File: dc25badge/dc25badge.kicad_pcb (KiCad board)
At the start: 2 copper layers, 111 parts, among them P1 BATT, P2 USB_OTG, P3 CONN_CORTEX, P4 UART, SW1 RESET, SW2 PWR, SW3 MODE, SW4 BRIGHT, U1 MIC5305, U10 APA102, U11 APA102, U12 APA102, U13 APA102, U14 APA102, U15 APA102, U16 APA102, U17 APA102, U18 APA102, U19 APA102, U2 TPS61232, U20 APA102, U21 APA102, U22 APA102, U23 APA102, U24 APA102, U25 APA102, U26 APA102, U27 APA102, U28 APA102, U29 APA102, U3 ATSAMD21E18A-AU, U30 APA102, U31 APA102, U32 APA102, U33 APA102, U34 APA102, U35 APA102, U36 APA102, U37 APA102, U38 APA102, U39 APA102, U4 74AHCT125, U40 APA102, U41 APA102, U42 APA102, U43 APA102, U44 APA102, U45 APA102, U46 APA102, U47 APA102, U48 APA102, U49 APA102, U5 APA102, U50 APA102, U51 APA102, U52 APA102, U53 APA102, U54 APA102, U55 APA102, U56 APA102, U57 APA102, U58 APA102, U59 APA102, U6 APA102, U60 APA102, U61 APA102, U62 APA102, U63 APA102, U64 APA102, U7 APA102, U8 APA102, U9 APA102, Y1 32.768k

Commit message: Full routing.
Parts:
- removed P4: UART, Pin_Headers2:Pin_Header_Straight_1x03_Pitch2.54mm_SMD_Pin1Left
- C15, C16, C17, C18, C19, C20, C21, C22, C23, C24, C25, C26, C8, R5, R6, SW1, SW2, SW3, SW4: moved to B.Cu
- moved C22 207.7 mm to (42.3, 28.8)
- moved C25 184.1 mm to (61.0, 57.1), turned to 270 degrees
- moved C23 178.7 mm to (48.4, 79.0)
- moved C26 174.5 mm to (52.2, 68.2), turned to 270 degrees
- moved C20 171.2 mm to (57.7, 79.0), turned to 180 degrees
- moved C15 148.7 mm to (101.2, 67.8), turned to 270 degrees
- moved C16 139.4 mm to (110.2, 56.9), turned to 270 degrees
- moved C17 132.2 mm to (96.9, 78.9)
- moved C18 131.9 mm to (137.8, 32.0)
- moved C19 127.8 mm to (106.7, 78.9), turned to 180 degrees
- moved SW4 116.3 mm to (68.7, 70.6)
- moved C21 111.2 mm to (161.7, 35.1), turned to 180 degrees
- moved SW1 100.6 mm to (101.2, 44.1), turned to 180 degrees
- moved C24 100.6 mm to (139.2, 83.8), turned to 180 degrees
- moved SW3 100.3 mm to (68.7, 62.4)
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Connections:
- net USBDM renamed USBD-
- net USBDP renamed USBD+
- P2 pad 6: Net-(P2-Pad6) -> GND
- U3 pad 25: Net-(U3-Pad25) -> 5V_EN
- U3 pad 5: 5V_EN -> Net-(U3-Pad5)
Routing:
- net +5V: track 34.2 -> 251.9 mm, vias 8 -> 30
- net 5V_EN: track 0.00 -> 95.0 mm, vias 0 -> 4
- net GND: track 112.9 -> 201.8 mm, vias 59 -> 60
- net /VBAT: track 0.00 -> 85.5 mm
- net +3V3: track 0.00 -> 59.4 mm
- net SPI_MOSI: track 0.00 -> 42.6 mm, vias 0 -> 1
- net BRIGHT: track 0.00 -> 37.6 mm
- net SPI_CLK: track 0.00 -> 35.6 mm, vias 0 -> 1
- net SPI_EN: track 0.00 -> 33.0 mm, vias 0 -> 2
- net MODE: track 0.00 -> 32.1 mm, vias 0 -> 2
- net ~RESET: track 0.00 -> 30.0 mm, vias 0 -> 2
- net Net-(R5-Pad2): track 0.00 -> 26.5 mm
- net SOFT_PWR: track 0.00 -> 23.1 mm, vias 0 -> 2
- net SCLK3: track 0.00 -> 17.9 mm
- net MOSI3: track 0.00 -> 16.7 mm
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- added copper zone on B.Cu, net +3V3
- added copper zone on B.Cu, net +5V
- added copper zone on B.Cu, net /VBAT
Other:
- rule trace_min: 0.254 -> 0.1524

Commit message: Gerbers.
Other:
- board outline added: 150.7 x 59.7 mm
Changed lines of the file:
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@@
     (links 358)
     (no_connects 0)
-    (area 0 0 0 0)
+    (area 26.344399 24.9826 177.683228 89.1374)
     (thickness 1.6)
-    (drawings 0)
+    (drawings 5)
     (tracks 1201)
     (zones 0)
@@
   (page A4)
   (layers
-    (0 F.Cu signal)
+    (0 F.Cu signal hide)
     (31 B.Cu signal)
     (32 B.Adhes user)
@@
     (visible_elements FFFFFF7F)
     (pcbplotparams
-      (layerselection 0x00030_80000001)
+      (layerselection 0x010f0_80000001)
       (usegerberextensions false)
       (excludeedgelayer true)
@@
       (plotinvisibletext false)
       (padsonsilk false)
-      (subtractmaskfromsilk false)
+      (subtractmaskfromsilk true)
       (outputformat 1)
       (mirror false)
-      (drillshape 1)
+      (drillshape 0)
       (scaleselection 1)
-      (outputdirectory ""))
+      (outputdirectory output/))
   )
   (net 0 "")
@@
     )
   )
+  (gr_line (start 26.67 86.868) (end 44.323 56.515) (angle 90) (layer Edge.Cuts) (width 0.15))
+  (gr_line (start 158.496 86.868) (end 26.67 86.868) (angle 90) (layer Edge.Cuts) (width 0.15))
+  (gr_line (start 177.419 27.178) (end 158.496 86.868) (angle 90) (layer Edge.Cuts) (width 0.15))
+  (gr_line (start 27.305 27.178) (end 177.419 27.178) (angle 90) (layer Edge.Cuts) (width 0.15))
+  (gr_line (start 44.323 56.515) (end 27.305 27.178) (angle 90) (layer Edge.Cuts) (width 0.15))
   (segment (start 78.008 31.369) (end 78.008 32.796) (width 0.254) (layer B.Cu) (net 1))
   (segment (start 78.008 32.796) (end 78.867 33.655) (width 0.254) (layer B.Cu) (net 1))

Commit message: PCB roll 1.
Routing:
- net GND: track 201.8 -> 242.4 mm
- net +5V: track 251.9 -> 257.1 mm, vias 30 -> 32
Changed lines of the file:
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@@
     (links 358)
     (no_connects 0)
-    (area 26.344399 24.9826 177.683228 89.1374)
+    (area 26.594999 27.102999 177.494001 86.943001)
     (thickness 1.6)
     (drawings 5)
-    (tracks 1201)
+    (tracks 1221)
     (zones 0)
     (modules 110)
@@
   (page A4)
   (layers
-    (0 F.Cu signal hide)
+    (0 F.Cu signal)
     (31 B.Cu signal)
     (32 B.Adhes user)
@@
   )
   (setup
-    (last_trace_width 1.016)
+    (last_trace_width 0.762)
     (user_trace_width 0.1524)
     (user_trace_width 0.254)
@@
   (gr_line (start 27.305 27.178) (end 177.419 27.178) (angle 90) (layer Edge.Cuts) (width 0.15))
   (gr_line (start 44.323 56.515) (end 27.305 27.178) (angle 90) (layer Edge.Cuts) (width 0.15))
+  (segment (start 145.542 43.962) (end 143.51 43.962) (width 0.762) (layer B.Cu) (net 1) (status C00000))
+  (segment (start 147.574 43.962) (end 145.542 43.962) (width 0.762) (layer B.Cu) (net 1) (status C00000))
+  (segment (start 150.007 44.196) (end 147.808 44.196) (width 0.762) (layer B.Cu) (net 1) (status C00000))
+  (segment (start 147.808 44.196) (end 147.574 43.962) (width 0.762) (layer B.Cu) (net 1) (status C00000))
+  (segment (start 150.007 44.196) (end 150.007 41.883) (width 0.762) (layer B.Cu) (net 1) (status C00000))
+  (segment (start 150.007 41.883) (end 149.907 41.783) (width 0.762) (layer B.Cu) (net 1) (status C00000))
+  (segment (start 151.257 47.498) (end 151.257 45.446) (width 0.762) (layer B.Cu) (net 1) (status 400000))
+  (segment (start 151.257 45.446) (end 150.007 44.196) (width 0.762) (layer B.Cu) (net 1) (status 800000))
+  (segment (start 151.257 47.498) (end 151.257 55.245) (width 1.016) (layer B.Cu) (net 1) (status 400000))
+  (segment (start 156.337 54.991) (end 156.337 50.018) (width 1.016) (layer B.Cu) (net 1) (status 800000))
+  (segment (start 156.464 55.118) (end 156.337 54.991) (width 1.016) (layer B.Cu) (net 1))
+  (segment (start 151.384 55.118) (end 156.464 55.118) (width 1.016) (layer B.Cu) (net 1))
+  (segment (start 151.257 55.245) (end 151.384 55.118) (width 1.016) (layer B.Cu) (net 1))
+  (segment (start 69.918 41.878) (end 74.2 41.878) (width 0.508) (layer B.Cu) (net 1) (status 400000))
+  (segment (start 76.6 39.478) (end 78.418 39.478) (width 0.508) (layer B.Cu) (net 1) (status 800000))
+  (segment (start 74.2 41.878) (end 76.6 39.478) (width 0.508) (layer B.Cu) (net 1))
   (segment (start 78.008 31.369) (end 78.008 32.796) (width 0.254) (layer B.Cu) (net 1))
   (segment (start 78.008 32.796) (end 78.867 33.655) (width 0.254) (layer B.Cu) (net 1))
@@
   (segment (start 84.639 41.078) (end 85.267 41.078) (width 0.508) (layer B.Cu) (net 3))
   (segment (start 85.267 41.078) (end 86.487 39.858) (width 0.508) (layer B.Cu) (net 3))
+  (segment (start 145.288 51.816) (end 145.288 54.61) (width 1.016) (layer B.Cu) (net 4) (status 400000))
+  (via (at 145.288 54.61) (size 1.016) (drill 0.508) (layers F.Cu B.Cu) (net 4))
+  (segment (start 145.288 51.816) (end 145.288 48.006) (width 1.016) (layer B.Cu) (net 4) (status 400000))
+  (via (at 143.891 49.276) (size 1.016) (drill 0.508) (layers F.Cu B.Cu) (net 4))
+  (segment (start 138.175 49.95) (end 139.153 49.95) (width 1.016) (layer F.Cu) (net 4) (status 400000))
+  (segment (start 138.946 43.95) (end 141.859 46.863) (width 0.508) (layer F.Cu) (net 4))
+  (via (at 141.859 46.863) (size 1.016) (drill 0.508) (layers F.Cu B.Cu) (net 4))
+  (segment (start 138.946 43.95) (end 136.675 43.95) (width 0.508) (layer F.Cu) (net 4))
+  (segment (start 141.859 47.244) (end 141.859 46.863) (width 1.016) (layer B.Cu) (net 4))
+  (segment (start 140.335 48.768) (end 141.859 47.244) (width 1.016) (layer B.Cu) (net 4))
+  (via (at 140.335 48.768) (size 1.016) (drill 0.508) (layers F.Cu B.Cu) (net 4))
+  (segment (start 139.153 49.95) (end 140.335 48.768) (width 1.016) (layer F.Cu) (net 4))
   (segment (start 140.569 83.693) (end 142.621 83.693) (width 1.016) (layer B.Cu) (net 4))
   (segment (start 146.431 79.883) (end 142.621 83.693) (width 2.54) (layer B.Cu) (net 4))
@@
   (segment (start 145.288 51.816) (end 145.288 49.276) (width 0.508) (layer B.Cu) (net 4))
   (segment (start 145.288 48.24) (end 143.51 46.462) (width 0.508) (layer B.Cu) (net 4))
-  (segment (start 136.675 43.95) (end 138.946 43.95) (width 0.508) (layer F.Cu) (net 4))
-  (via (at 141.859 46.863) (size 1.016) (drill 0.508) (layers F.Cu B.Cu) (net 4))
-  (segment (start 138.946 43.95) (end 141.859 46.863) (width 0.508) (layer F.Cu) (net 4))
   (segment (start 138.175 49.95) (end 141.312 49.95) (width 0.508) (layer F.Cu) (net 4))
   (via (at 141.986 49.276) (size 1.016) (drill 0.508) (layers F.Cu B.Cu) (net 4))
@@
   (segment (start 104.002 58.05) (end 104.013 58.039) (width 1.016) (layer F.Cu) (net 4))
   (segment (start 51.175 55.95) (end 49.346 55.95) (width 1.016) (layer F.Cu) (net 4))
-  (segment (start 45.223 58.05) (end 46.825 58.05) (width 1.016) (layer F.Cu) (net 4))
-  (segment (start 45.212 58.039) (end 45.223 58.05) (width 0.508) (layer F.Cu) (net 4))
-  (via (at 45.212 58.039) (size 1.016) (drill 0.508) (layers F.Cu B.Cu) (net 4))
-  (segment (start 47.117 58.039) (end 45.212 58.039) (width 1.016) (layer B.Cu) (net 4))
-  (segment (start 49.276 55.88) (end 47.117 58.039) (width 1.016) (layer B.Cu) (net 4))
   (via (at 49.276 55.88) (size 1.016) (drill 0.508) (layers F.Cu B.Cu) (net 4))
   (segment (start 49.346 55.95) (end 49.276 55.88) (width 0.508) (layer F.Cu) (net 4))

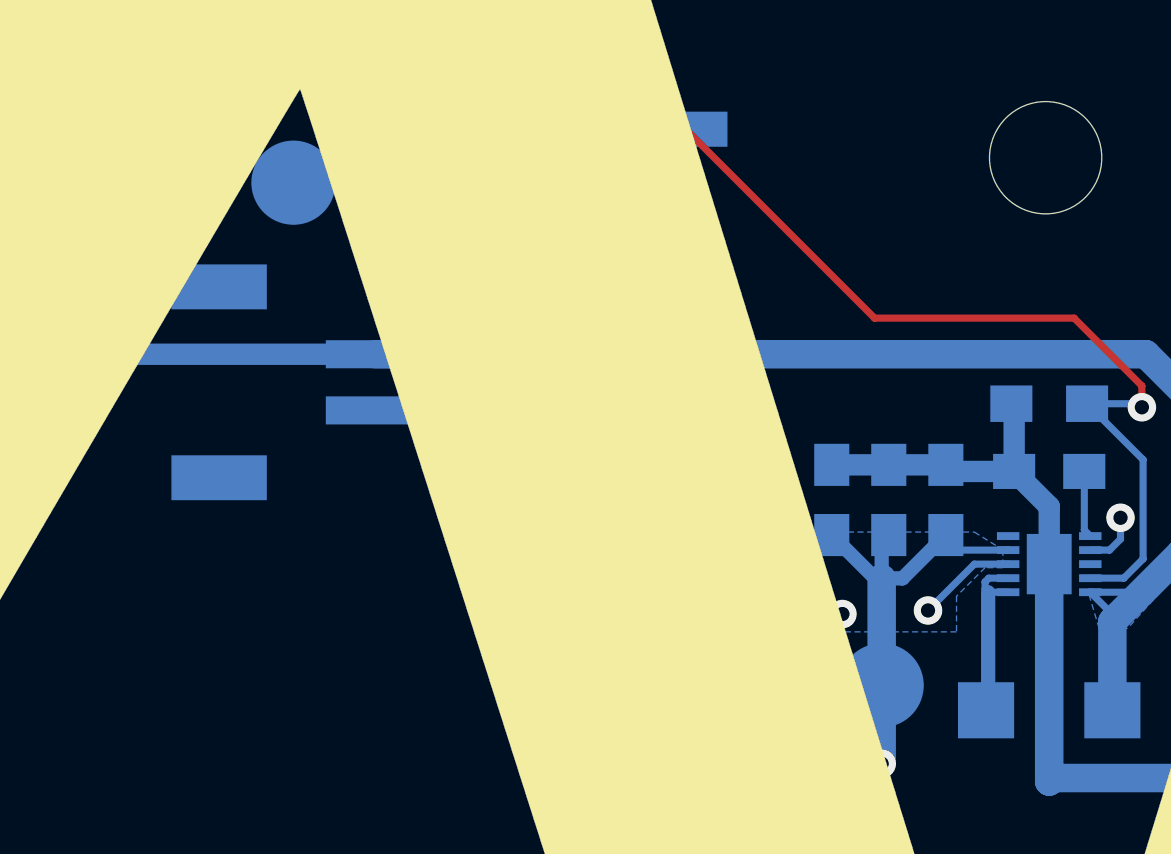
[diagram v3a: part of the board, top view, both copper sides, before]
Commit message: Fix battery error.
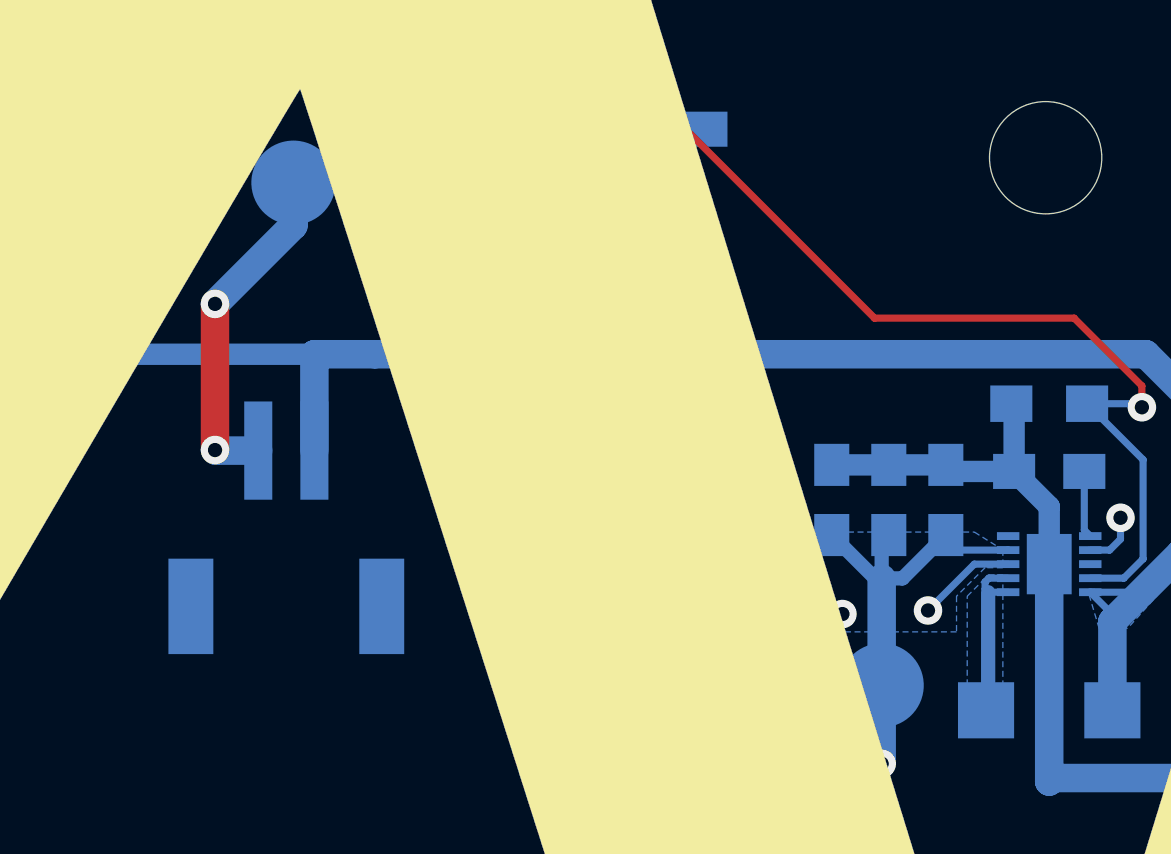
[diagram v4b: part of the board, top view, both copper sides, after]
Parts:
- moved P1 5.22 mm to (124.1, 46.2), turned to 180 degrees
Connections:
- P1 pad 1: GND -> /VBAT
- P1 pad 2: /VBAT -> GND
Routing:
- net GND: track 242.4 -> 254.6 mm, vias 60 -> 62
- net /VBAT: track 85.5 -> 91.1 mm
- net +5V: vias 32 -> 31
- net (no net): vias 0 -> 1
- added copper zone on B.Cu, net Net-(L1-Pad2)
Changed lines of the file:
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@@
     (thickness 1.6)
     (drawings 5)
-    (tracks 1221)
+    (tracks 1230)
     (zones 0)
     (modules 110)
@@
   )
   (setup
-    (last_trace_width 0.762)
+    (last_trace_width 1.016)
     (user_trace_width 0.1524)
     (user_trace_width 0.254)
@@
   )
   (module Connectors_JST:JST_PH_S2B-PH-SM4-TB_02x2.00mm_Angled (layer B.Cu)
-    (at 124.46 41.021 90)
+    (at 124.079 46.228 180)
     (descr http://www.jst-mfg.com/product/pdf/eng/ePH.pdf)
     (tags "connector jst ph")
     (attr smd)
-    (fp_text reference P1 (at -1.5 6 90) (layer B.SilkS)
+    (fp_text reference P1 (at -1.5 6 180) (layer B.SilkS) hide
       (effects (font (size 1 1) (thickness 0.15)) (justify mirror))
     )
-    (fp_text value BATT (at 0 -6 90) (layer B.Fab)
+    (fp_text value BATT (at 0 -6 180) (layer B.SilkS)
       (effects (font (size 1 1) (thickness 0.15)) (justify mirror))
     )
@@
     (fp_line (start 4.7 5.05) (end 4.7 -5) (layer B.CrtYd) (width 0.05))
     (fp_line (start 4.7 -5) (end -4.7 -5) (layer B.CrtYd) (width 0.05))
-    (pad 1 smd rect (at -1 2.775 90) (size 1 3.5) (layers B.Cu B.Paste B.Mask)
-      (net 1 GND))
-    (pad 2 smd rect (at 1 2.775 90) (size 1 3.5) (layers B.Cu B.Paste B.Mask)
+    (pad 1 smd rect (at -1 2.775 180) (size 1 3.5) (layers B.Cu B.Paste B.Mask)
       (net 157 /VBAT))
-    (pad "" smd rect (at -3.4 -2.775 90) (size 1.6 3.4) (layers B.Cu B.Paste B.Mask))
-    (pad "" smd rect (at 3.4 -2.775 90) (size 1.6 3.4) (layers B.Cu B.Paste B.Mask))
+    (pad 2 smd rect (at 1 2.775 180) (size 1 3.5) (layers B.Cu B.Paste B.Mask)
+      (net 1 GND))
+    (pad "" smd rect (at -3.4 -2.775 180) (size 1.6 3.4) (layers B.Cu B.Paste B.Mask))
+    (pad "" smd rect (at 3.4 -2.775 180) (size 1.6 3.4) (layers B.Cu B.Paste B.Mask))
   )
   (module Resistors_SMD:R_0805_HandSoldering (layer B.Cu)
@@
   (gr_line (start 27.305 27.178) (end 177.419 27.178) (angle 90) (layer Edge.Cuts) (width 0.15))
   (gr_line (start 44.323 56.515) (end 27.305 27.178) (angle 90) (layer Edge.Cuts) (width 0.15))
-  (segment (start 145.542 43.962) (end 143.51 43.962) (width 0.762) (layer B.Cu) (net 1) (status C00000))
-  (segment (start 147.574 43.962) (end 145.542 43.962) (width 0.762) (layer B.Cu) (net 1) (status C00000))
-  (segment (start 150.007 44.196) (end 147.808 44.196) (width 0.762) (layer B.Cu) (net 1) (status C00000))
-  (segment (start 147.808 44.196) (end 147.574 43.962) (width 0.762) (layer B.Cu) (net 1) (status C00000))
-  (segment (start 150.007 44.196) (end 150.007 41.883) (width 0.762) (layer B.Cu) (net 1) (status C00000))
-  (segment (start 150.007 41.883) (end 149.907 41.783) (width 0.762) (layer B.Cu) (net 1) (status C00000))
-  (segment (start 151.257 47.498) (end 151.257 45.446) (width 0.762) (layer B.Cu) (net 1) (status 400000))
-  (segment (start 151.257 45.446) (end 150.007 44.196) (width 0.762) (layer B.Cu) (net 1) (status 800000))
-  (segment (start 151.257 47.498) (end 151.257 55.245) (width 1.016) (layer B.Cu) (net 1) (status 400000))
-  (segment (start 156.337 54.991) (end 156.337 50.018) (width 1.016) (layer B.Cu) (net 1) (status 800000))
+  (via (at 143.891 49.276) (size 1.016) (drill 0.508) (layers F.Cu B.Cu) (net 0))
+  (segment (start 123.079 43.453) (end 121.558 43.453) (width 1.016) (layer B.Cu) (net 1) (status 400000))
+  (segment (start 124.333 35.433) (end 124.333 33.909) (width 1.016) (layer B.Cu) (net 1) (status 800000))
+  (segment (start 121.539 38.227) (end 124.333 35.433) (width 1.016) (layer B.Cu) (net 1))
+  (via (at 121.539 38.227) (size 1.016) (drill 0.508) (layers F.Cu B.Cu) (net 1))
+  (segment (start 121.539 43.434) (end 121.539 38.227) (width 1.016) (layer F.Cu) (net 1))
+  (via (at 121.539 43.434) (size 1.016) (drill 0.508) (layers F.Cu B.Cu) (net 1))
+  (segment (start 121.558 43.453) (end 121.539 43.434) (width 1.016) (layer B.Cu) (net 1))
+  (segment (start 145.542 43.962) (end 143.51 43.962) (width 0.762) (layer B.Cu) (net 1))
+  (segment (start 147.574 43.962) (end 145.542 43.962) (width 0.762) (layer B.Cu) (net 1))
+  (segment (start 150.007 44.196) (end 147.808 44.196) (width 0.762) (layer B.Cu) (net 1))
+  (segment (start 147.808 44.196) (end 147.574 43.962) (width 0.762) (layer B.Cu) (net 1))
+  (segment (start 150.007 44.196) (end 150.007 41.883) (width 0.762) (layer B.Cu) (net 1))
+  (segment (start 150.007 41.883) (end 149.907 41.783) (width 0.762) (layer B.Cu) (net 1))
+  (segment (start 151.257 47.498) (end 151.257 45.446) (width 0.762) (layer B.Cu) (net 1))
+  (segment (start 151.257 45.446) (end 150.007 44.196) (width 0.762) (layer B.Cu) (net 1))
+  (segment (start 151.257 47.498) (end 151.257 55.245) (width 1.016) (layer B.Cu) (net 1))
+  (segment (start 156.337 54.991) (end 156.337 50.018) (width 1.016) (layer B.Cu) (net 1))
   (segment (start 156.464 55.118) (end 156.337 54.991) (width 1.016) (layer B.Cu) (net 1))
   (segment (start 151.384 55.118) (end 156.464 55.118) (width 1.016) (layer B.Cu) (net 1))
   (segment (start 151.257 55.245) (end 151.384 55.118) (width 1.016) (layer B.Cu) (net 1))
-  (segment (start 69.918 41.878) (end 74.2 41.878) (width 0.508) (layer B.Cu) (net 1) (status 400000))
-  (segment (start 76.6 39.478) (end 78.418 39.478) (width 0.508) (layer B.Cu) (net 1) (status 800000))
+  (segment (start 69.918 41.878) (end 74.2 41.878) (width 0.508) (layer B.Cu) (net 1))
+  (segment (start 76.6 39.478) (end 78.418 39.478) (width 0.508) (layer B.Cu) (net 1))
   (segment (start 74.2 41.878) (end 76.6 39.478) (width 0.508) (layer B.Cu) (net 1))
   (segment (start 78.008 31.369) (end 78.008 32.796) (width 0.254) (layer B.Cu) (net 1))
@@
   (segment (start 84.639 41.078) (end 85.267 41.078) (width 0.508) (layer B.Cu) (net 3))
   (segment (start 85.267 41.078) (end 86.487 39.858) (width 0.508) (layer B.Cu) (net 3))
-  (segment (start 145.288 51.816) (end 145.288 54.61) (width 1.016) (layer B.Cu) (net 4) (status 400000))
+  (segment (start 145.288 51.816) (end 145.288 54.61) (width 1.016) (layer B.Cu) (net 4))
   (via (at 145.288 54.61) (size 1.016) (drill 0.508) (layers F.Cu B.Cu) (net 4))
-  (segment (start 145.288 51.816) (end 145.288 48.006) (width 1.016) (layer B.Cu) (net 4) (status 400000))
-  (via (at 143.891 49.276) (size 1.016) (drill 0.508) (layers F.Cu B.Cu) (net 4))
-  (segment (start 138.175 49.95) (end 139.153 49.95) (width 1.016) (layer F.Cu) (net 4) (status 400000))
+  (segment (start 145.288 51.816) (end 145.288 48.006) (width 1.016) (layer B.Cu) (net 4))
+  (segment (start 138.175 49.95) (end 139.153 49.95) (width 1.016) (layer F.Cu) (net 4))
   (segment (start 138.946 43.95) (end 141.859 46.863) (width 0.508) (layer F.Cu) (net 4))
   (via (at 141.859 46.863) (size 1.016) (drill 0.508) (layers F.Cu B.Cu) (net 4))
@@
   (segment (start 149.175 82.15) (end 151.825 82.15) (width 0.254) (layer F.Cu) (net 151))
   (segment (start 149.175 84) (end 151.825 84) (width 0.254) (layer F.Cu) (net 152))
+  (segment (start 125.079 43.453) (end 125.079 40.021) (width 1.016) (layer B.Cu) (net 157) (status 400000))
+  (segment (start 125.079 40.021) (end 127.235 40.021) (width 1.016) (layer B.Cu) (net 157))
+  (segment (start 127.235 40.021) (end 105.954 40.021) (width 0.762) (layer B.Cu) (net 157))
+  (segment (start 127.235 40.021) (end 154.702 40.021) (width 1.016) (layer B.Cu) (net 157))
+  (segment (start 154.702 40.021) (end 157.861 43.18) (width 1.016) (layer B.Cu) (net 157))
+  (segment (start 157.861 43.18) (end 157.861 46.228) (width 1.016) (layer B.Cu) (net 157))
   (segment (start 153.507 49.546) (end 153.507 49.2855) (width 0.254) (layer B.Cu) (net 157))
   (segment (start 153.507 49.546) (end 155.956 47.097) (width 1.016) (layer B.Cu) (net 157))
@@
   (segment (start 97.366 34.737) (end 99.228 34.737) (width 0.762) (layer B.Cu) (net 157))
   (segment (start 99.228 34.737) (end 99.949 34.016) (width 0.762) (layer B.Cu) (net 157))
-  (segment (start 127.235 40.021) (end 105.954 40.021) (width 0.762) (layer B.Cu) (net 157))
   (segment (start 105.954 40.021) (end 99.949 34.016) (width 0.762) (layer B.Cu) (net 157))
   (segment (start 153.507 52.705) (end 153.507 49.546) (width 1.016) (layer B.Cu) (net 157))
-  (segment (start 127.235 40.021) (end 154.702 40.021) (width 1.016) (layer B.Cu) (net 157))
-  (segment (start 154.702 40.021) (end 157.861 43.18) (width 1.016) (layer B.Cu) (net 157))
-  (segment (start 157.861 43.18) (end 157.861 46.228) (width 1.016) (layer B.Cu) (net 157))
   (segment (start 157.861 46.228) (end 156.992 47.097) (width 1.016) (layer B.Cu) (net 157))
   (segment (start 153.416 52.614) (end 153.507 52.705) (width 0.508) (layer B.Cu) (net 157))
@@
       )
     )
+  )
+  (zone (net 159) (net_name "Net-(L1-Pad2)") (layer B.Cu) (hatch edge 0.508)
+    (priority 5)
+    (connect_pads yes (clearance 0.254))
+    (min_thickness 0.254)
+    (fill yes (arc_segments 16) (thermal_gap 0.254) (thermal_bridge_width 0.508))
+    (polygon
+      (pts
+        (xy 149.606 51.816) (xy 148.336 51.816) (xy 148.336 48.641) (xy 149.098 47.879) (xy 149.606 47.879)
+      )
+    )
